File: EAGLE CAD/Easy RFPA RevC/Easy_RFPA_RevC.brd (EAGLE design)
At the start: 127 x 147.3 mm, 284 parts, among them IC1 LM741D, IC2 LM741D, IC3 LM393D, IC5 74AHC1G00DBV, IC6 74LS74D, IC7 74AHC1G86DBV, J401 HDR_2X1282836-1282836-1, J402 KK_PCFAN, Q1 IRF630, Q101 IRF520N, Q102 IRF630, Q2 MOSFET_NBSS123SOT23, Q201 IRF630, Q202 IRF630, Q3 NPNMMBT3904SOT23_BEC, Q301 MOSFET_NBSS123SOT23, Q302 PNPSOT23_BEC, Q303 NPNMMBT3904SOT23_BEC, Q4 PNPSOT23_BEC, SW1 SPST_NO_TACT_RA43125608371643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, SW2 SPST_NO_TACT_RA43125608371643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, T1 HP1_TRAFO, T102 HP4_TRAFO, U1 OPAMP_QUADTLV274IDSOIC14, U302 OPAMP_QUADTLV274IDSOIC14, U401 LDO_3TERMMC78M12CTGTO220_VERT, U402 LDO_3TERMMC78M05CTGTO220_VERT, X1 1-227161-0, X2 1-227161-0, X4 1-227161-0, X402 HEATSINK_OMNI_DUALOMNI-UNI-30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

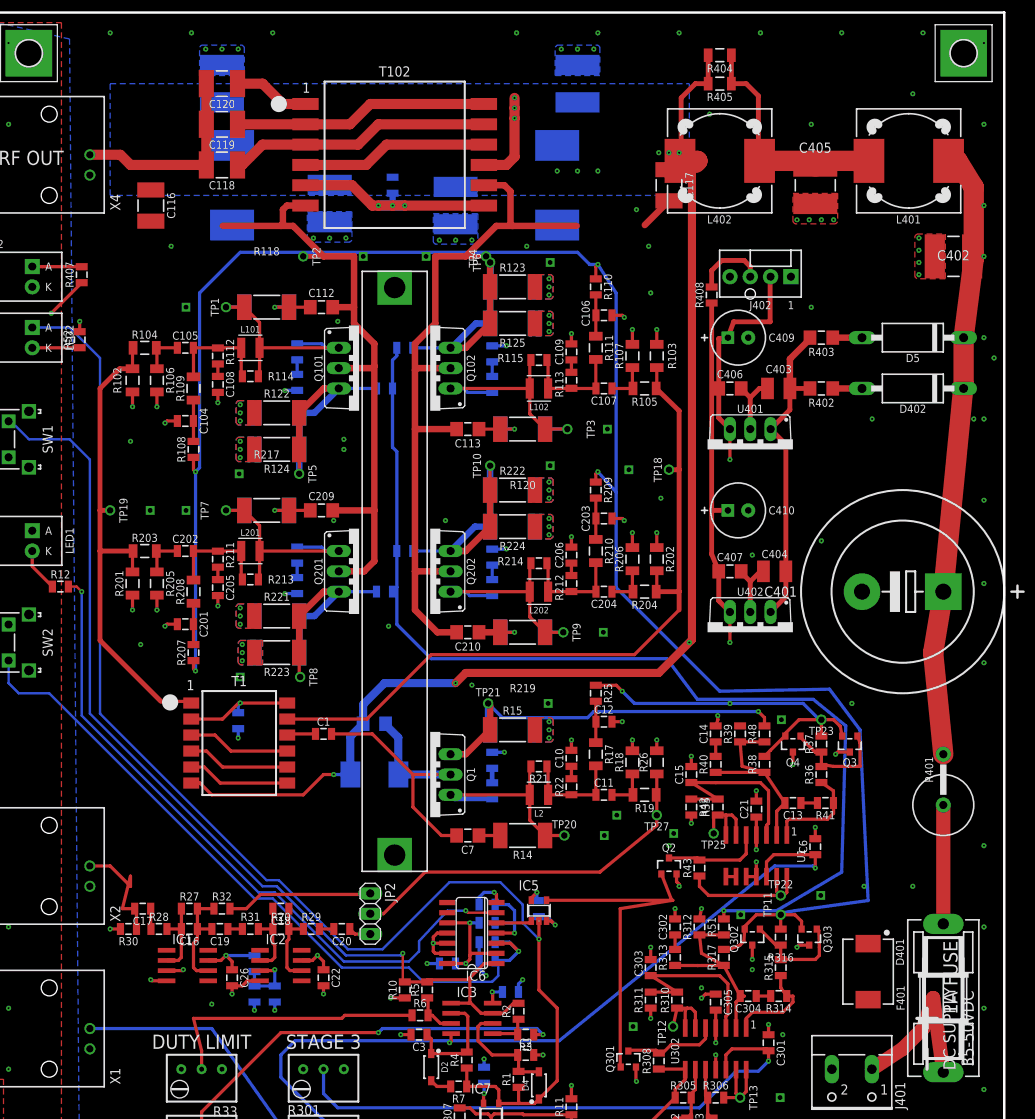
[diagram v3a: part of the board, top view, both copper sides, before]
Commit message: Slip around S2 layout
Fits better with surroundings
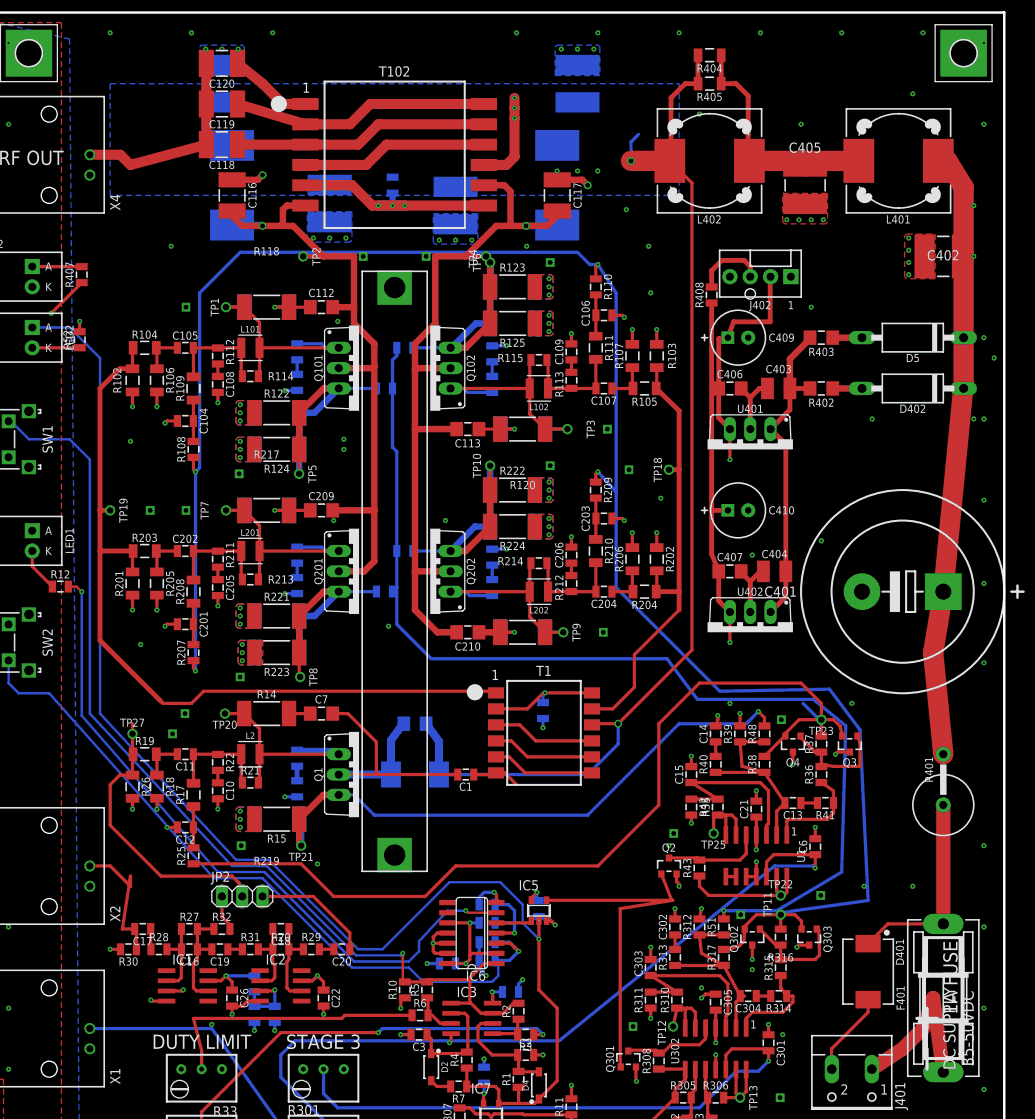
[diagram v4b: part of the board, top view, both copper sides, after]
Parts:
- moved TP27 66.3 mm to (18.0, 49.5), turned to 0 degrees
- moved R26 65.6 mm to (18.0, 42.9), turned to 270 degrees
- moved R19 62.7 mm to (19.6, 47.0), turned to 0 degrees
- moved R18 59.5 mm to (21.1, 42.9), turned to 270 degrees
- moved R25 54.2 mm to (25.7, 34.3), turned to 90 degrees
- moved C12 54.0 mm to (24.6, 37.8), turned to 180 degrees
- moved C11 52.6 mm to (24.6, 47.0), turned to 180 degrees
- moved R17 50.5 mm to (25.7, 41.9), turned to 90 degrees
- moved TP20 45.1 mm to (29.6, 52.1), turned to 180 degrees
- moved C10 44.4 mm to (28.7, 42.4), turned to 270 degrees
- moved R22 44.3 mm to (28.7, 46.0), turned to 270 degrees
- moved R101 38.1 mm to (69.3, 52.5)
- moved T1 38.1 mm to (69.5, 49.7)
- moved L2 36.4 mm to (32.8, 47.0), turned to 0 degrees
- moved R21 36.1 mm to (32.8, 43.4), turned to 0 degrees
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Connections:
- removed net S1_DN: C1.1, T1.10
- new net N$49: C1.1, T1.6
- net VB: now also T1.10; no longer T1.6
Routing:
- net S2_GBIAS: track 45.2 -> 118.6 mm, vias 1 -> 0
- net ABP1: track 61.9 -> 100.8 mm
- net ABN1: track 93.0 -> 56.7 mm
- net S1_BP5: track 50.0 -> 74.0 mm
- net +5V: track 213.4 -> 229.6 mm
- net N$76: track 18.3 -> 4.48 mm
- net GND: track 141.0 -> 153.2 mm
- net N$74: track 2.82 -> 14.8 mm
- net S2_BP1: track 46.6 -> 35.8 mm
- net N$44: track 14.9 -> 25.3 mm
- net VB: track 153.5 -> 144.4 mm, vias 8 -> 7
- net N$49: track 0.00 -> 6.05 mm
- net DRAINS_POS: track 82.3 -> 86.0 mm, vias 0 -> 1
- net S1_DN: track 3.60 -> 0.00 mm
- net N$69: track 15.8 -> 18.3 mm
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
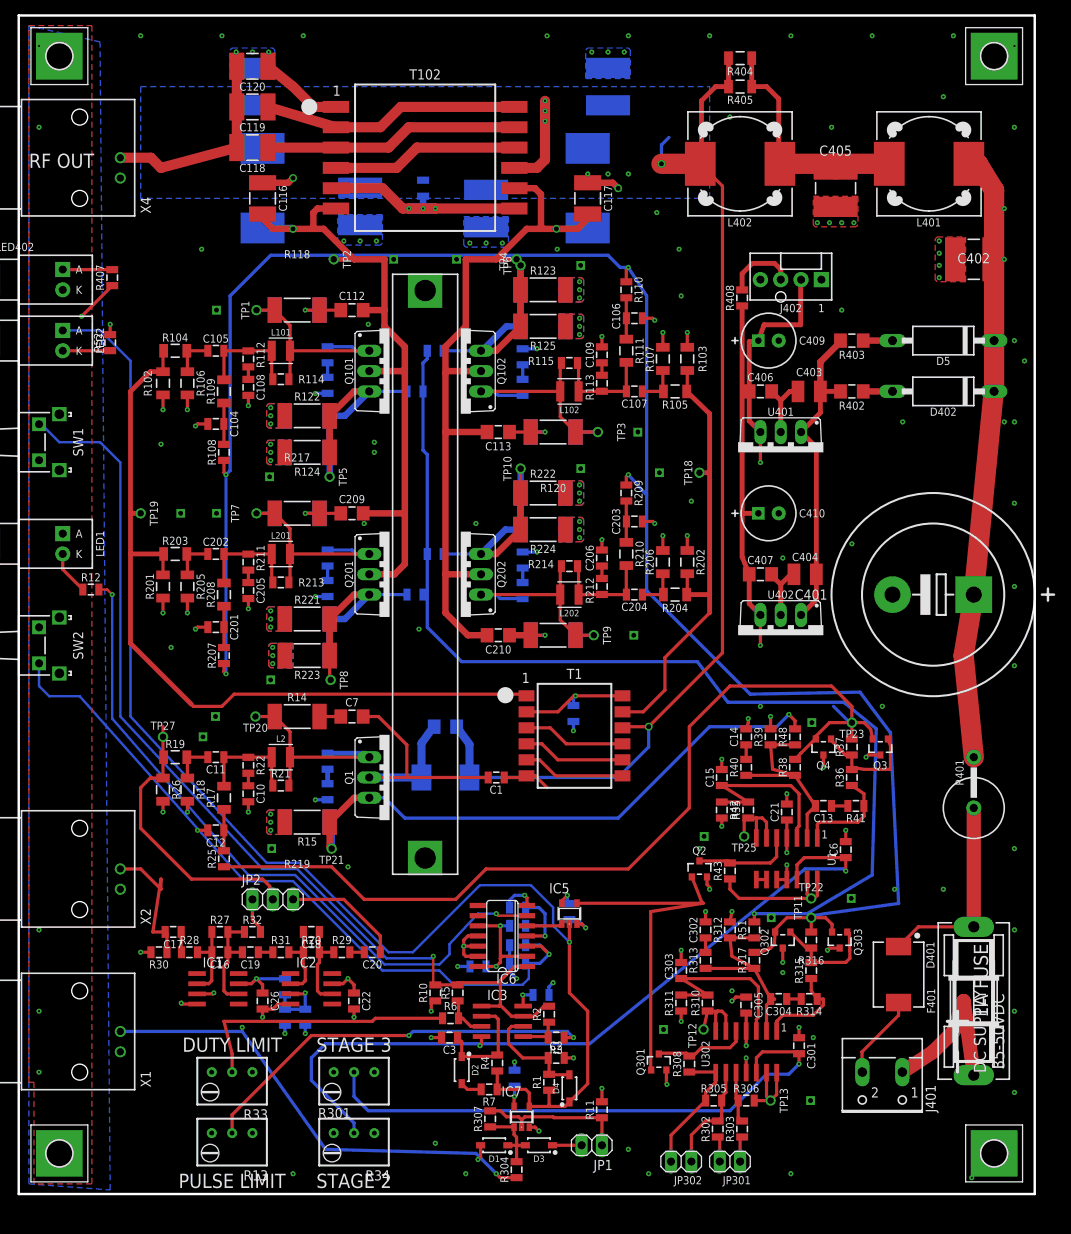
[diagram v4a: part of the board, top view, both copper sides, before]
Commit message: cleaning up revC
fixed all major DRC errors
returned all nets to default class
all airwires routed
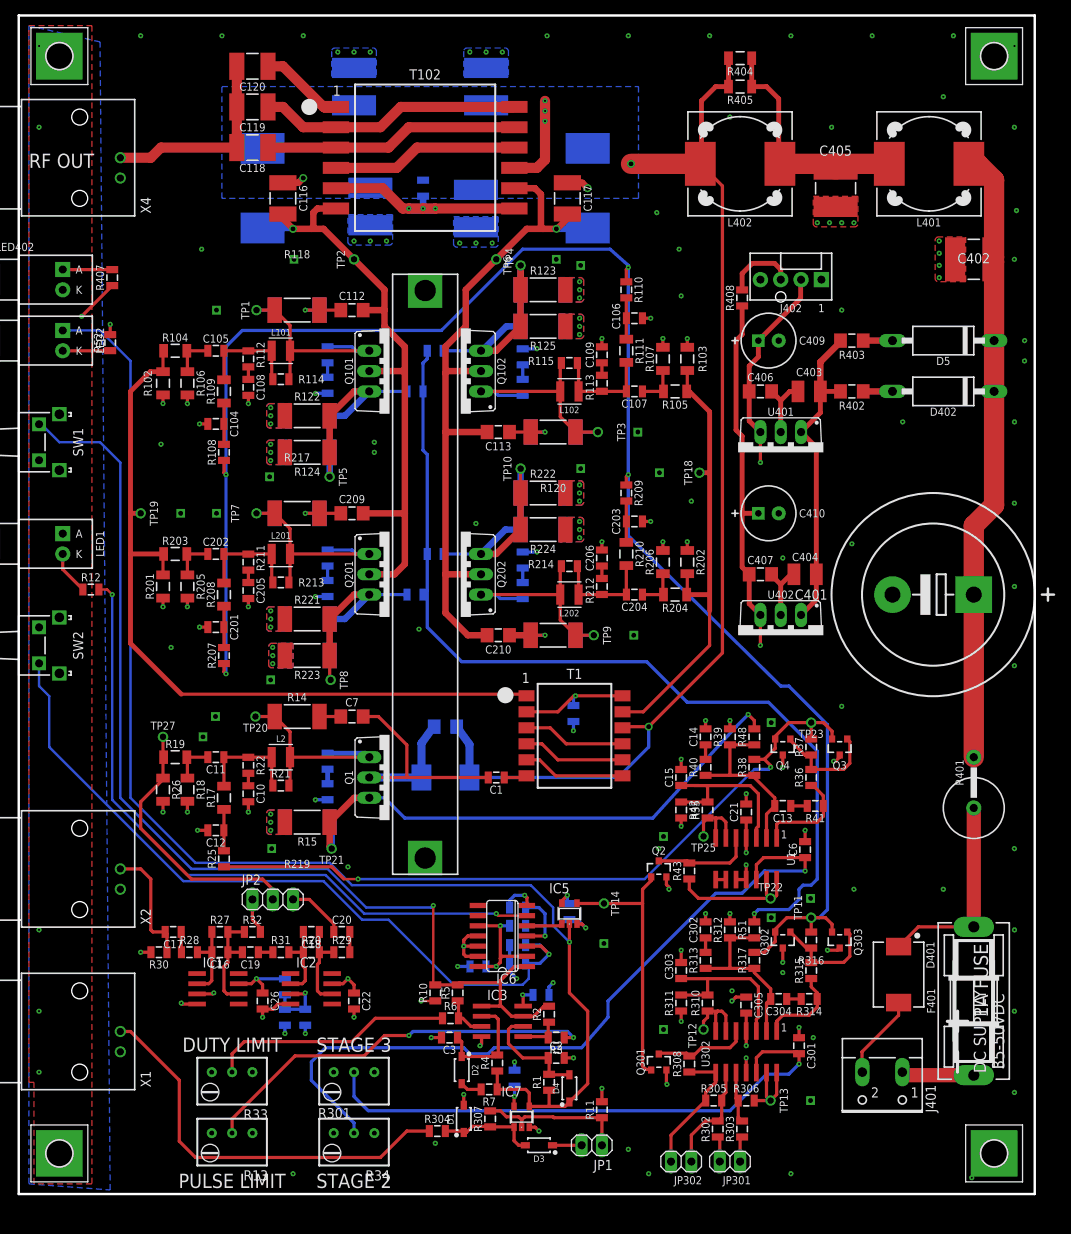
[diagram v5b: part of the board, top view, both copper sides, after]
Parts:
- added TP14: PROBE_TPTP_5MM, MDT_CON:PROBE_TP_5MM
- moved C413 15.2 mm to (58.4, 130.8)
- moved C412 12.7 mm to (41.9, 130.8)
- moved R304 11.0 mm to (52.3, 0.25), turned to 0 degrees
- moved R35 5.08 mm to (86.1, 40.4)
- moved R38 5.08 mm to (91.9, 45.7)
- moved R43 5.08 mm to (83.8, 32.8)
- moved R48 5.08 mm to (91.9, 49.5)
- moved C13 5.08 mm to (95.5, 40.9)
- moved C14 5.08 mm to (85.9, 49.5)
- moved C15 5.08 mm to (82.8, 44.5)
- moved C21 5.08 mm to (90.9, 40.1)
- moved C6 5.08 mm to (98.3, 35.4)
- moved Q2 5.08 mm to (80.0, 33.0)
- moved Q3 5.08 mm to (102.6, 48.3)
- moved Q4 5.08 mm to (95.5, 48.3)
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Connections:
- net !BLANK_GATED: now also TP14.TP
- net GND: now also TP14.GND
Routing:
- net +12V: track 132.4 -> 73.7 mm
- net S2_GBIAS: track 118.6 -> 92.0 mm, vias 0 -> 2
- net S3_GBIAS: track 237.4 -> 213.1 mm
- net N$22: track 132.8 -> 118.4 mm
- net N$45: track 21.6 -> 9.09 mm
- net !BLANK_GATED: track 45.8 -> 33.6 mm
- net GND: track 153.2 -> 141.7 mm, vias 180 -> 173
- net !FAULT: track 124.9 -> 133.9 mm
- net N$74: track 14.8 -> 7.37 mm
- net N$53: track 58.4 -> 51.0 mm, vias 1 -> 0
- net DRAINS_POS: track 86.0 -> 78.7 mm
- net DRAINS_NEG: track 98.3 -> 91.0 mm
- net +5V: track 229.6 -> 235.1 mm
- net S1_BP5: track 74.0 -> 69.2 mm
- net N$68: track 34.3 -> 30.8 mm
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
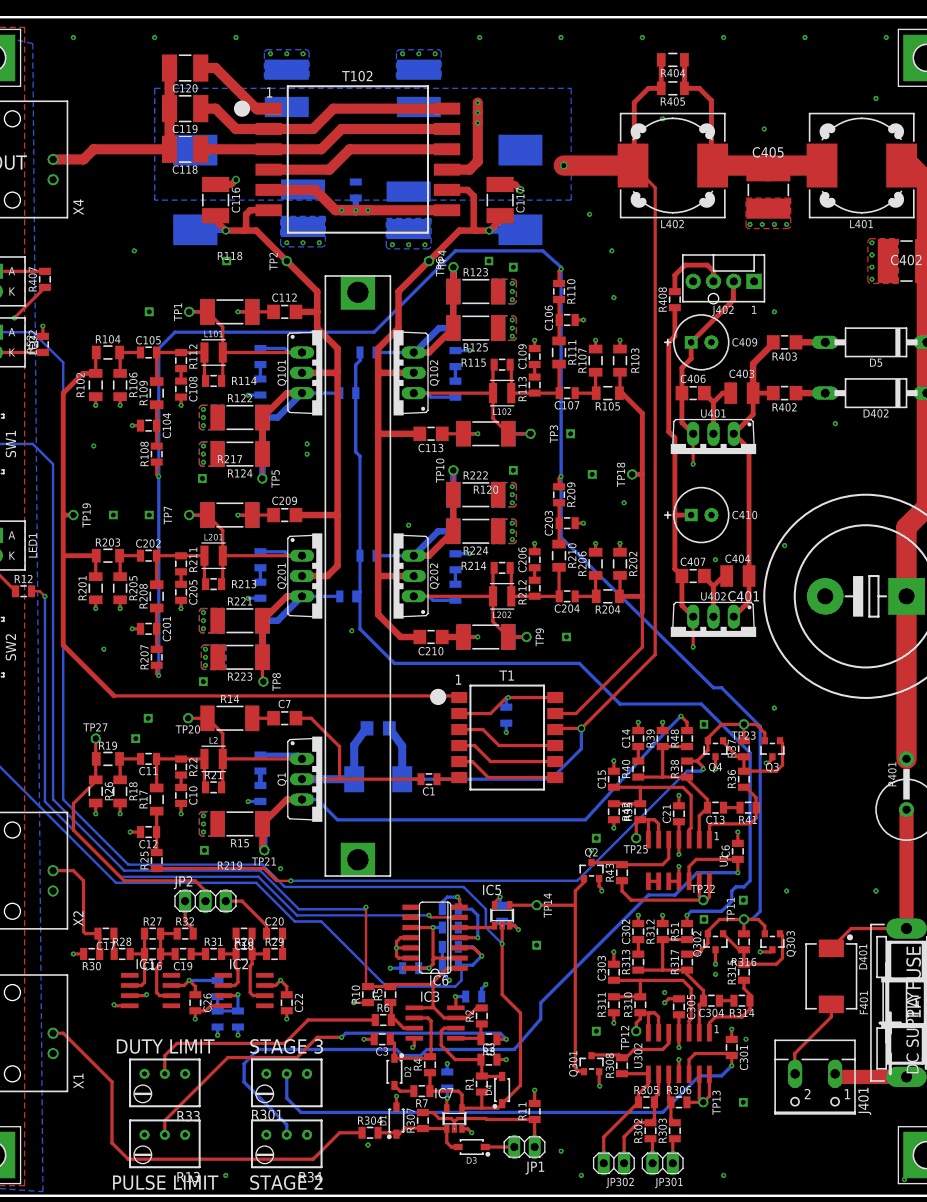
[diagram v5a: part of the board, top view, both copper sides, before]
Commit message: Output balun section
To save space, remove C119 and C120, replace with 1206 resistors instead to select turns ratio
Put all drain bias inductors back on top side
Add keepouts to inductor packages
Move R44-47 to centerline, away from FETs
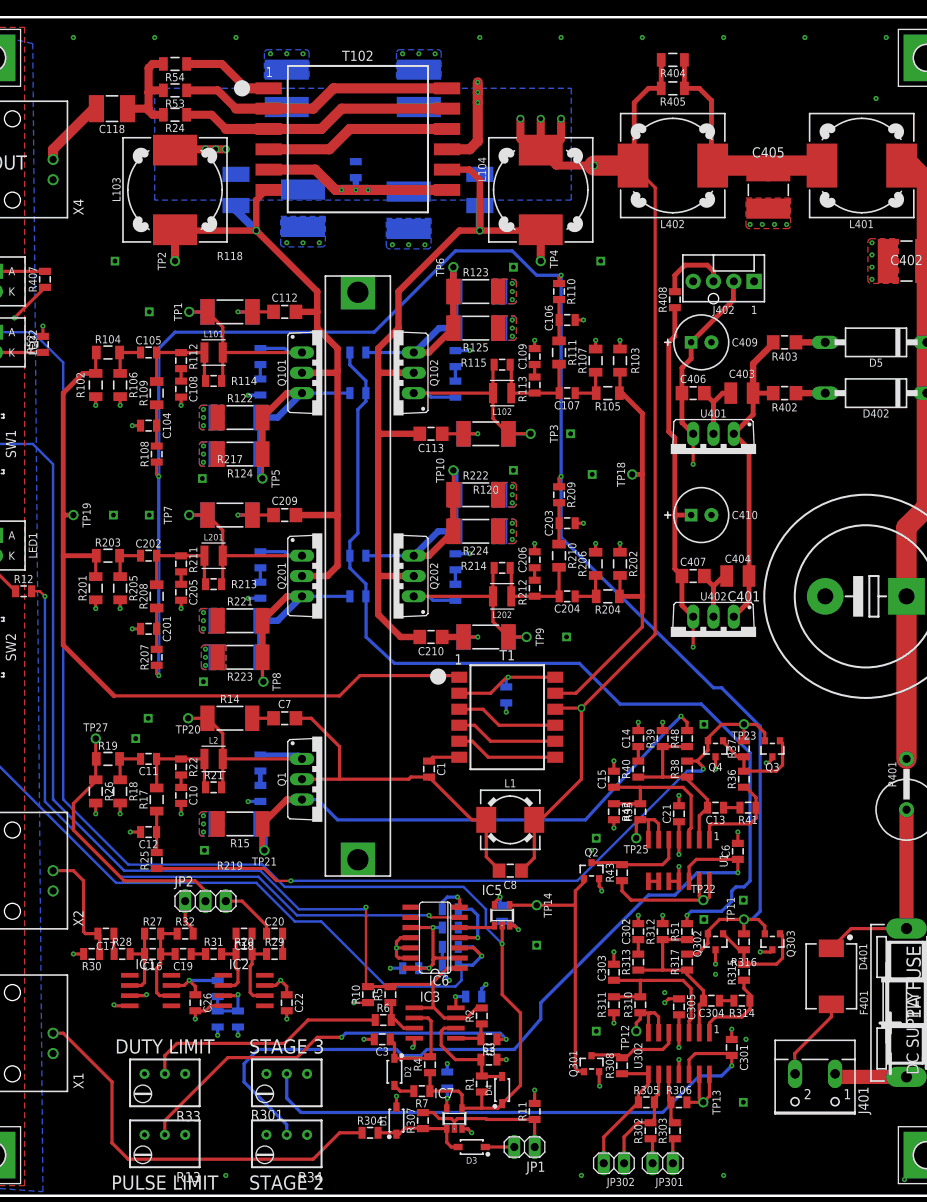
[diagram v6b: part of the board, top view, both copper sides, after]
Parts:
- removed C119: DNP, MDT_C:C1812
- removed C120: 3nF, MDT_C:C1812
- added R24, R53, R54: 0, MDT_R:1206_IPC-7351B
- moved C8 24.3 mm to (69.8, 33.0), flipped to the top, turned to 180 degrees
- moved L1 17.3 mm to (69.8, 39.4), flipped to the top, turned to 0 degrees
- moved TP4 14.0 mm to (73.7, 109.2)
- moved TP2 14.0 mm to (27.9, 109.2)
- moved C118 10.5 mm to (20.1, 128.3)
- moved C116 2.84 mm to (35.6, 118.1), flipped to the bottom
- moved C117 2.84 mm to (66.0, 118.1), flipped to the bottom
- moved R132 2.54 mm to (50.5, 120.7)
- moved T1 2.54 mm to (69.5, 52.2)
- moved L103 2.54 mm to (27.9, 118.1), flipped to the top
- moved R101 2.54 mm to (69.3, 55.0)
- moved L104 2.54 mm to (73.7, 118.1), flipped to the top
- moved T102 2.54 mm to (50.8, 124.5)
- moved R45 1.27 mm to (50.8, 97.8)
- moved R47 1.27 mm to (50.8, 72.4)
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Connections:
- new net N$85: C118.1, R24.2, R53.2, R54.2
- net N$29: now also R53.1; no longer C119.1
- net N$30: now also R54.1; no longer C120.1
- net N$31: no longer C119.2, C120.2
- net N$52: now also R24.1; no longer C118.1
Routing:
- net N$31: track 25.2 -> 8.79 mm
- net N$85: track 0.00 -> 14.0 mm
- net DRAINS_NEG: track 91.0 -> 101.0 mm
- net DRAINS_POS: track 78.7 -> 87.9 mm
- net VB: track 142.0 -> 149.6 mm, vias 4 -> 8
- net S2_DP: track 39.5 -> 43.6 mm
- net ABN1: track 56.9 -> 54.3 mm
- net N$52: track 31.8 -> 34.3 mm
- net BN5: track 32.4 -> 34.3 mm
- net AN5: track 35.4 -> 37.2 mm
- net N$29: track 32.9 -> 34.6 mm
- net AP5: track 32.4 -> 34.0 mm
- net BP5: track 29.4 -> 30.9 mm
- net S3_GBIAS: track 213.1 -> 211.8 mm
- net N$49: track 2.86 -> 3.98 mm
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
